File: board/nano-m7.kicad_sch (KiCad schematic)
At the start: 36 parts, among them J1 Z-FORCE, J10 UI PANEL, J11 HDMI POWER, J12 RASPI, J2 Z-STEPPER, J3 Z-STOP LOW, J4 LAMP NTC, J5 LAMP PWM, J6 LAMP FAN, J7 LAMP FAN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

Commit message: WIP
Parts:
- R3: value 270R -> 330R
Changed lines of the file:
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@@
 			)
 		)
-		(property "Value" "270R"
+		(property "Value" "330R"
 			(at 189.23 105.41 90)
 			(effects

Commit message: WIP
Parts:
- C1, C2: value 22p -> 18p
- Y1: value 12MHz -> 16MHz
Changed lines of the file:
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@@
 			)
 		)
-		(property "Value" "22p"
+		(property "Value" "18p"
 			(at 39.624 58.928 90)
 			(effects
@@
 			)
 		)
-		(property "Value" "22p"
+		(property "Value" "18p"
 			(at 39.624 50.038 90)
 			(effects
@@
 			)
 		)
-		(property "Value" "12MHz"
+		(property "Value" "16MHz"
 			(at 47.498 54.61 90)
 			(effects

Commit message: Add notes on new 5V source and LDO requirements to schematic
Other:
- note added: "upravy: - nový zdroj 5V - 3V3 stačí LDO (LM1117)"
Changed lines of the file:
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@@
 	(generator_version "9.0")
 	(paper "A4")
+	(text "upravy:\n- nový zdroj 5V\n- 3V3 stačí LDO (LM1117)\n"
+		(exclude_from_sim no)
+		(at 106.172 97.028 0)
+		(effects
+			(font
+				(size 1.27 1.27)
+			)
+			(justify left)
+		)
+	)
 	(junction
 		(at 50.8 45.72)

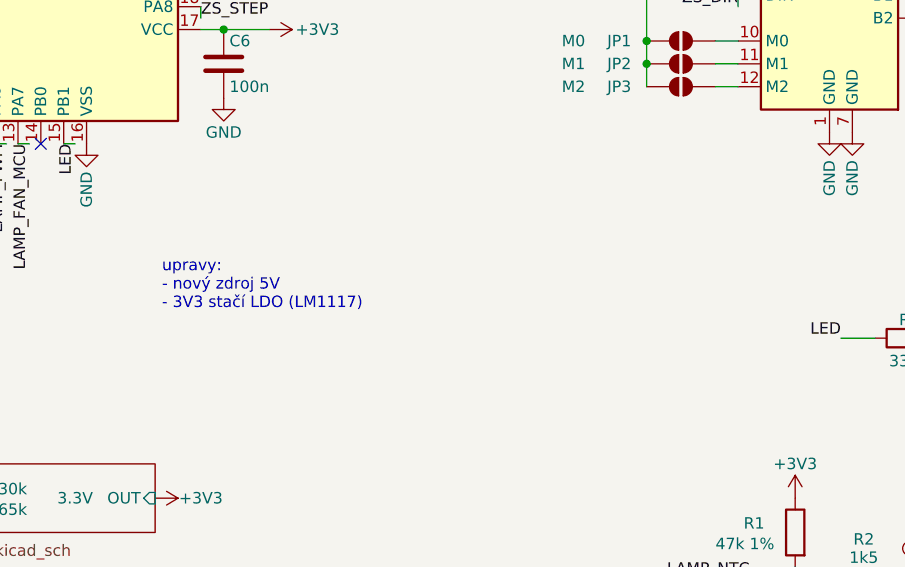
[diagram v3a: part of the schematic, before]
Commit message: Enhance Z-axis functionality with stepper motor control and ISR integration; update front panel button configuration
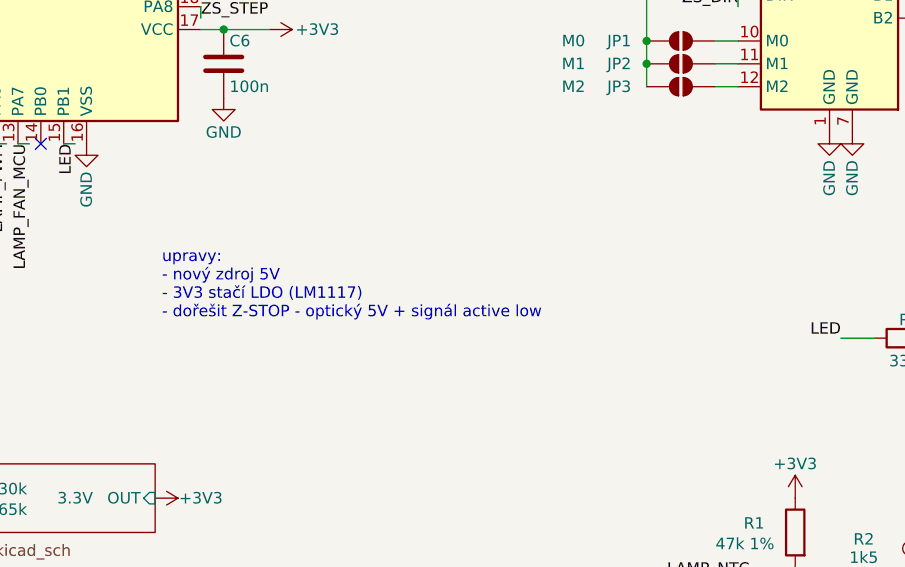
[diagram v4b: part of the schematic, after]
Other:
- note added: "upravy: - nový zdroj 5V - 3V3 stačí LDO (LM1117) - dořešit Z-STOP - optický 5V + signál active low"
- note removed: "upravy: - nový zdroj 5V - 3V3 stačí LDO (LM1117)"
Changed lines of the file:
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@@
 	(generator_version "9.0")
 	(paper "A4")
-	(text "upravy:\n- nový zdroj 5V\n- 3V3 stačí LDO (LM1117)\n"
+	(text "upravy:\n- nový zdroj 5V\n- 3V3 stačí LDO (LM1117)\n- dořešit Z-STOP - optický 5V + signál active low\n"
 		(exclude_from_sim no)
 		(at 106.172 97.028 0)

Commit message: WIP
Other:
- note added: "upravy: - nový zdroj 5V - 3V3 stačí LDO (LM1117) - třípinový konektor na Z-STOP - optický 5V + signál active low - nEN pro stepper driver"
- note removed: "upravy: - nový zdroj 5V - 3V3 stačí LDO (LM1117) - dořešit Z-STOP - optický 5V + signál active low"
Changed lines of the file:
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@@
 	(generator_version "9.0")
 	(paper "A4")
-	(text "upravy:\n- nový zdroj 5V\n- 3V3 stačí LDO (LM1117)\n- dořešit Z-STOP - optický 5V + signál active low\n"
+	(text "upravy:\n- nový zdroj 5V\n- 3V3 stačí LDO (LM1117)\n- třípinový konektor na Z-STOP - optický 5V + signál active low\n- nEN pro stepper driver\n\n"
 		(exclude_from_sim no)
 		(at 106.172 97.028 0)

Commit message: WIP
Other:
- note added: "upravy: - nový zdroj 5V - 3V3 stačí LDO (LM1117) - třípinový konektor na Z-STOP - optický 5V + signál active low - nEN pro stepper driver (na PA15?)"
- note removed: "upravy: - nový zdroj 5V - 3V3 stačí LDO (LM1117) - třípinový konektor na Z-STOP - optický 5V + signál active low - nEN pro stepper driver"
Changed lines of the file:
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@@
 	(generator_version "9.0")
 	(paper "A4")
-	(text "upravy:\n- nový zdroj 5V\n- 3V3 stačí LDO (LM1117)\n- třípinový konektor na Z-STOP - optický 5V + signál active low\n- nEN pro stepper driver\n\n"
+	(text "upravy:\n- nový zdroj 5V\n- 3V3 stačí LDO (LM1117)\n- třípinový konektor na Z-STOP - optický 5V + signál active low\n- nEN pro stepper driver (na PA15?)\n\n"
 		(exclude_from_sim no)
 		(at 106.172 97.028 0)

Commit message: 1.1
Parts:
- added C12, C13: 10u, Capacitor_SMD:C_0805_2012Metric, symbol Device:C
- added C6: 100u/35V, Capacitor_SMD:CP_Elec_6.3x5.8, symbol Device:C_Polarized
- added C7: 100n, Capacitor_SMD:C_0805_2012Metric, symbol Device:C
- added C9: 100u/16V, Capacitor_SMD:CP_Elec_6.3x5.8, symbol Device:C_Polarized
- added D1: SS24, Diode_SMD:D_SMA_Handsoldering, symbol Device:D_Schottky_Small
- added L1: 47uH/2A, Inductor_SMD:L_Sunlord_MWSA0604S, symbol Device:L
- added U2: XL1509-5.0, Package_SO:SOIC-8_3.9x4.9mm_P1.27mm, symbol Regulator_Switching:XL1509-5.0
- added U3: LM1117MP-3.3, Package_TO_SOT_SMD:SOT-223-3_TabPin2, symbol Regulator_Linear:LM1117MP-3.3
- C11: renamed from C8; footprint Capacitor_SMD:C_0805_2012Metric_Pad1.18x1.45mm_HandSolder -> Capacitor_SMD:C_0805_2012Metric
- J3: footprint Connector_JST:JST_XH_B2B-XH-A_1x02_P2.50mm_Vertical -> Connector_JST:JST_XH_B3B-XH-A_1x03_P2.50mm_Vertical; symbol Connector_Generic:Conn_01x02 -> Connector_Generic:Conn_01x03
- R1, R2: footprint Resistor_SMD:R_0805_2012Metric_Pad1.20x1.40mm_HandSolder -> Resistor_SMD:R_0805_2012Metric
- renumbered C7 to C10, C6 to C8, D1 to D2
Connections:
- net +24V: now also C6.1, C7.1, U2.1 (VIN)
- net +3V3: now also C13.1, U3.2 (VO)
- net +5V: now also J3.1 (Pin_1), C12.1, C9.1, L1.2, U2.3 (FB), U3.3 (VI)
- net GND: now also C12.2, C13.2, C6.2, C7.2, C9.2, D1.2 (A), U2.4 (~{EN}), U2.5 (GND), U2.6 (GND), U2.7 (GND), U2.8 (GND), U3.1 (GND)
- net Z_STOP_LOW: now also J3.3 (Pin_3); no longer J3.1 (Pin_1)
- net ~{ZS_FAULT}: now reaches A1.2 (~{FLT})
- net ~{ZS_FAULT}: now also U1.22 (PA12)
- net ~{ZS_EN}: now reaches A1.9 (~{EN})
- net ~{ZS_EN}: now also U1.21 (PA11)
- new net: D1.1 (K), L1.1, U2.2 (OUT)
- no-connect marks 10 -> 6
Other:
- removed sheet DCDC1
- removed sheet DCDC2
- note added: "upravy: - třípinový konektor na Z-STOP - optický 5V + signál active low"
- note removed: "upravy: - nový zdroj 5V - 3V3 stačí LDO (LM1117) - třípinový konektor na Z-STOP - optický 5V + signál active low - nEN pro stepper driver (na PA15?)"
- moved on the sheet: J1, J2, JP1, JP2, JP3

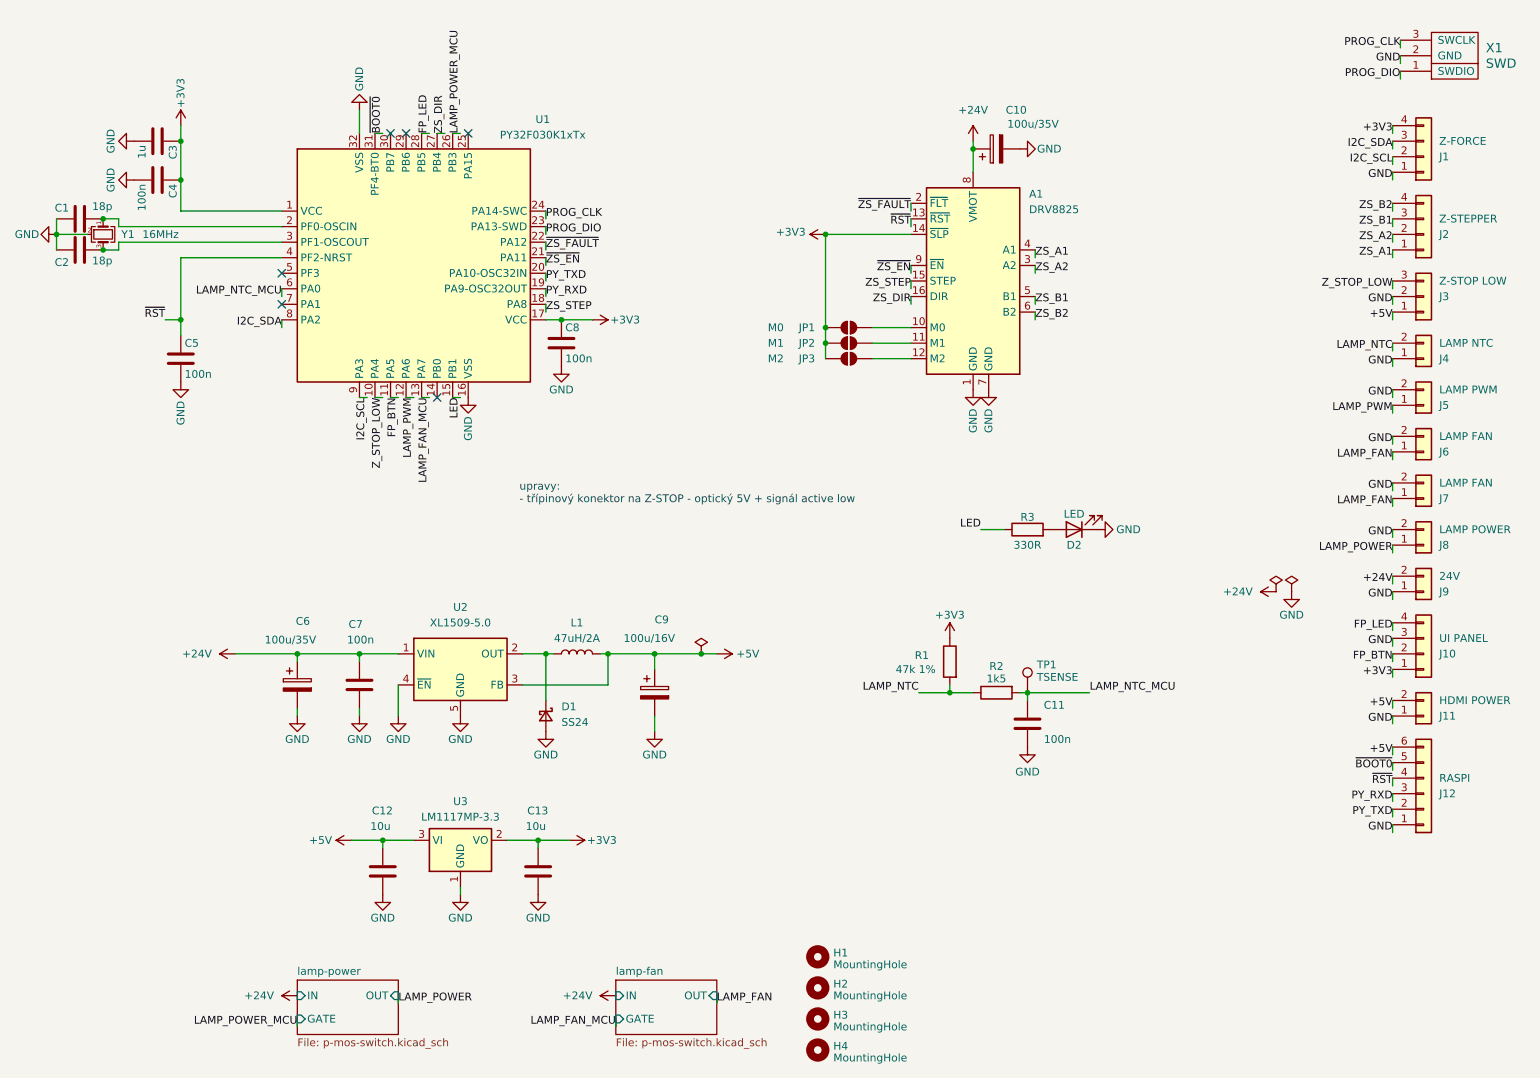
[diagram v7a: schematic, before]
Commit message: Update schematic text for next version 1.2 with hardware pull-up for ZS_EN
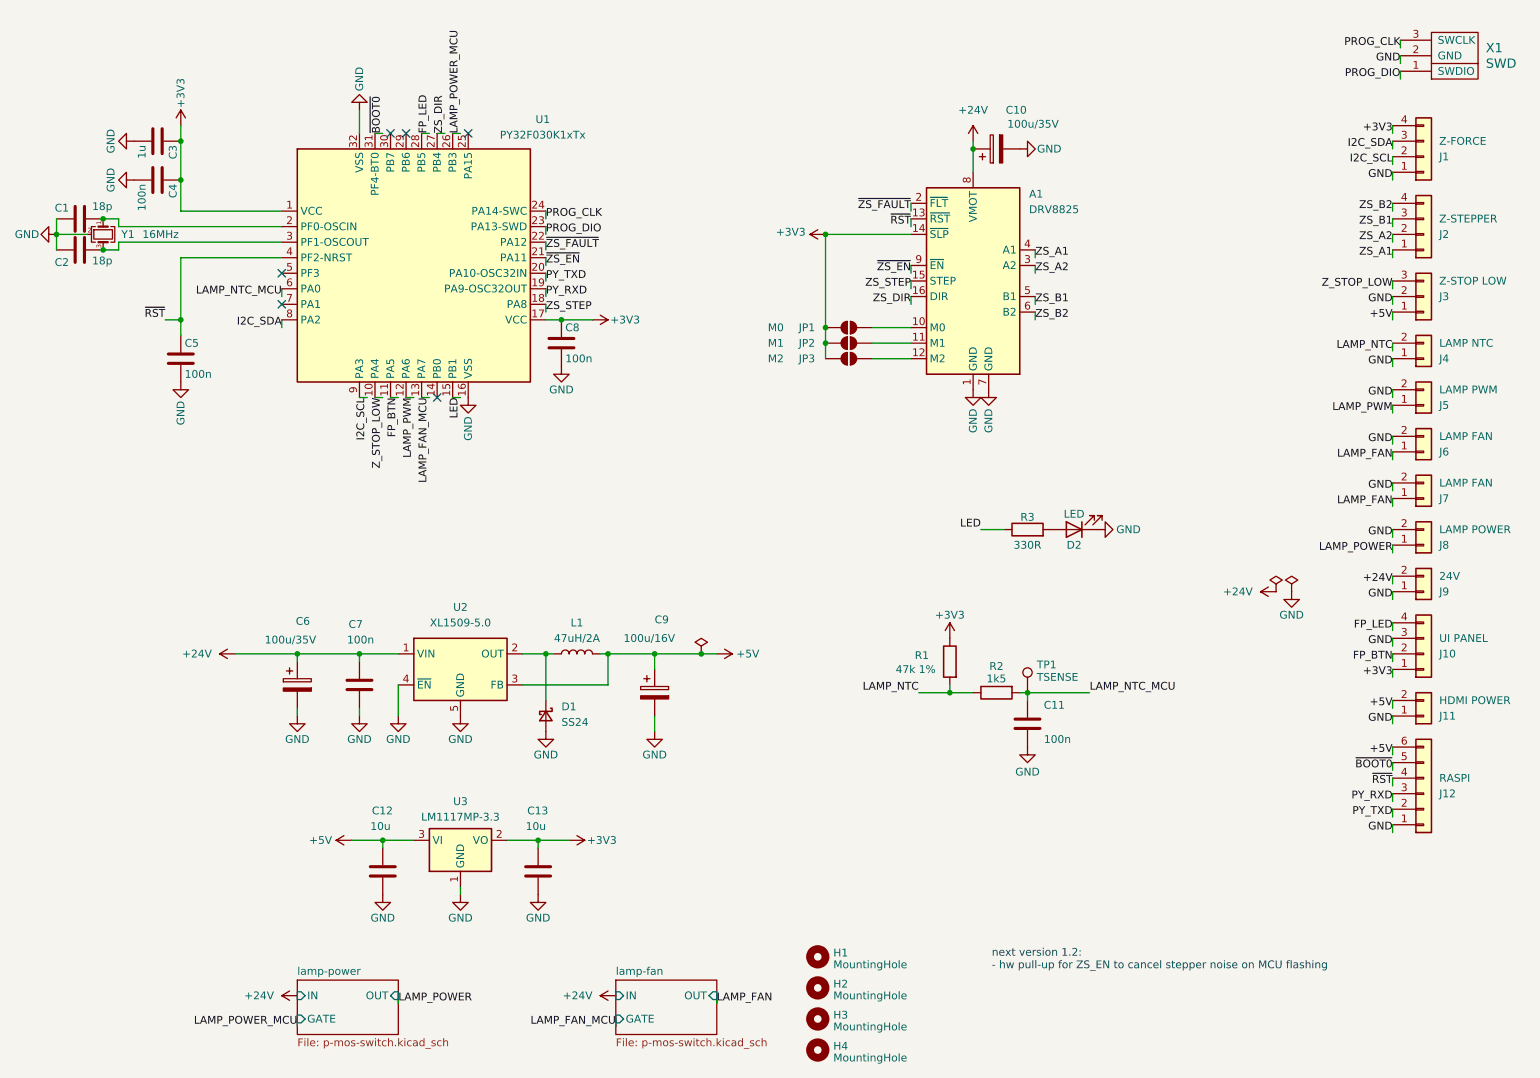
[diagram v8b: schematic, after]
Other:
- note added: "next version 1.2: - hw pull-up for ZS_EN to cancel stepper noise on MCU flashing"
- note removed: "upravy: - třípinový konektor na Z-STOP - optický 5V + signál active low"
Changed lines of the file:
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@@
 	(generator_version "9.0")
 	(paper "A4")
-	(text "upravy:\n- třípinový konektor na Z-STOP - optický 5V + signál active low"
+	(text "next version 1.2:\n- hw pull-up for ZS_EN to cancel stepper noise on MCU flashing"
 		(exclude_from_sim no)
-		(at 106.172 97.028 0)
+		(at 183.388 173.228 0)
 		(effects
 			(font
